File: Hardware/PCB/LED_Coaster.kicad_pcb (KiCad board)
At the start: 2 copper layers, 90 x 90 mm, 88 parts, among them J1 Li-po, J3 USB_C_Receptacle_USB2.0_16P, J4 UART, Q1 AO3401A, SW1 SW_SPDT, U1 ESP32-C3-WROOM-02-H4, U3 MCP73871-2CC, U4 TLV75533PDBVR

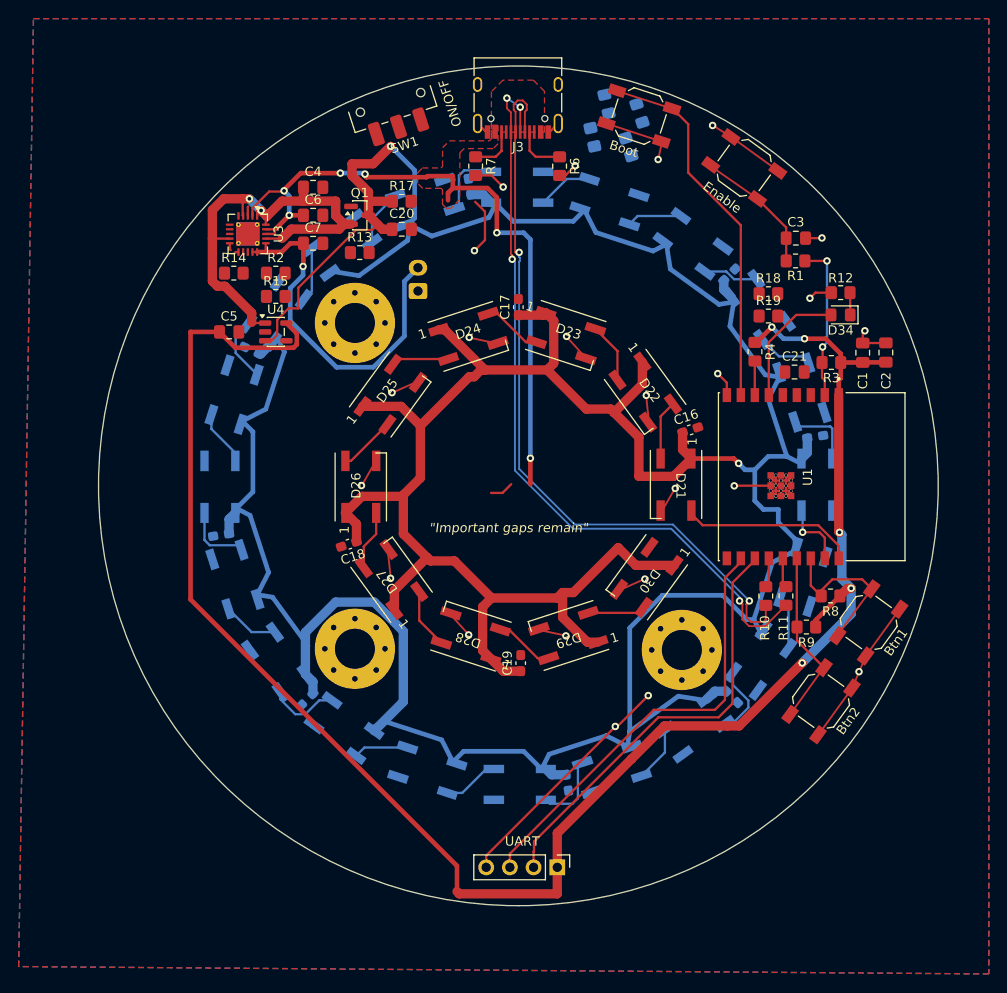
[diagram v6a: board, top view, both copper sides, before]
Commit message: Finish phase 5: route what was left and clean the board up
Every net with more than one pad is now one island, there are no
shorts, both LED chains are continuous, and the strays sweep is clean.

Routing:

- Action 8 in full - U3's three config resistors, the P-FET gate,
  R13 onto +SYS, both status LEDs across to R5/R16/D33/D35, and the
  battery-sense divider.
- A B.Cu link between J3's two VBUS pad pairs. They had only ever been
  joined by the priority-1 +5V zone, and when that zone shrank on a
  refill the status LEDs went with it - +5V split in two. The whole
  USB signal row sits between the pads and the F.Cu escapes below are
  taken by CC1, CC2 and the differential pairs, so the link runs
  underneath on B.Cu where there is nothing but the STAT2 run.
- U3 pad 3 down into U3's own exposed pad. Its old stub ran the other
  way and stopped 1.7 mm short of the pour, and the direct path to the
  pour crosses +SYS.

GND pad connection is now Solid, with thermal relief kept on J1, J3
and J4. Thermal relief was leaving eleven ground pads unconnected: the
pour was wrapped right around them at exactly thermal_gap, but the ring
traces block the spoke directions and KiCad places no spoke at all
rather than fewer than min_resolved_spokes. Reflow does not care about
solid pads; the three parts that get hand-soldered keep their relief.

min_copper_edge_clearance goes from 0.0 to 0.3 so the rule can actually
fail.

Also strips 14 items of junk copper: 12 zero-length segments and two
dangling stubs. All verified against connectivity before removal.

Co-Authored-By: Claude Opus 5 <noreply@anthropic.com>
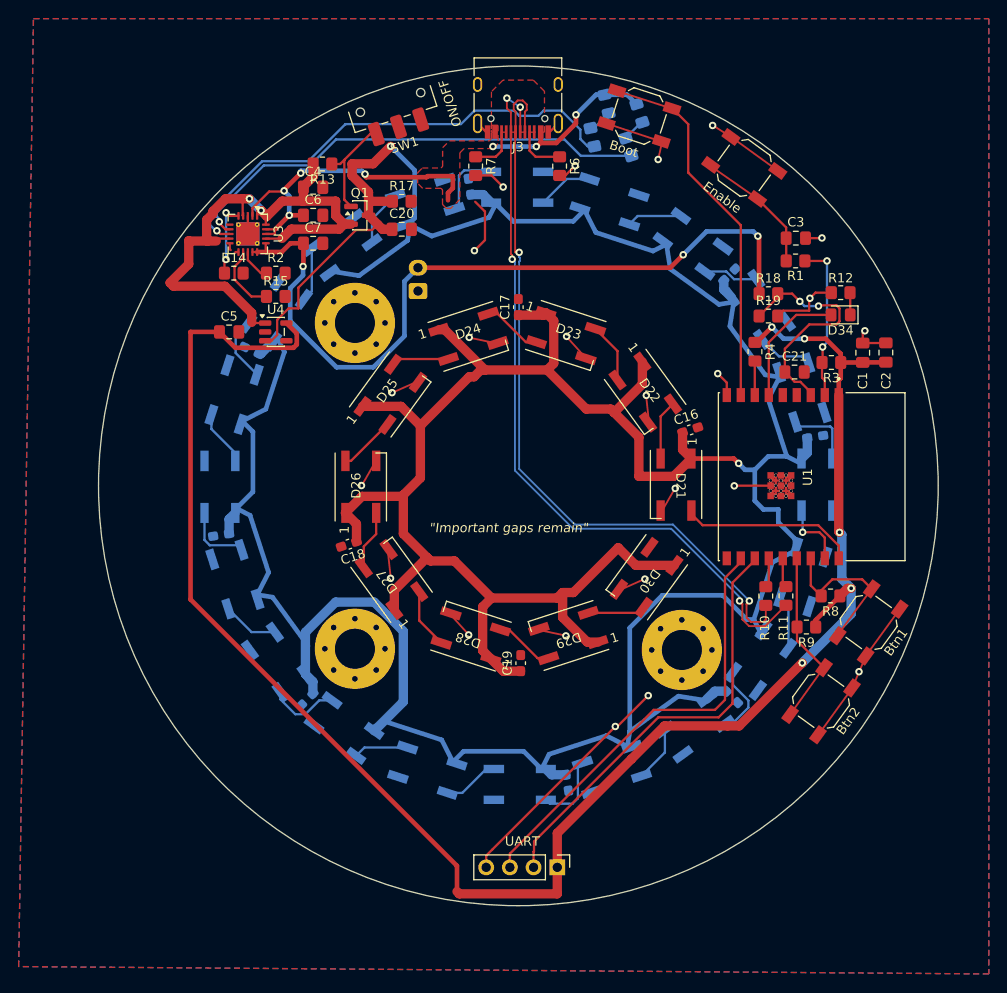
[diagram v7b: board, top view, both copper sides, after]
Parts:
- moved R13 10.3 mm to (129.0, 45.5), turned to 180 degrees
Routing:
- net Net-(U3-STAT1/~{LBO}): track 0.00 -> 52.3 mm, vias 0 -> 1
- net Net-(U3-STAT2): track 0.00 -> 51.1 mm, vias 0 -> 1
- net +BATT: track 39.4 -> 83.9 mm, vias 1 -> 3
- net /BAT_SENSE: track 0.00 -> 25.5 mm, vias 0 -> 2
- net +5V: track 75.2 -> 56.4 mm, vias 6 -> 7
- net Net-(Q1-G): track 0.00 -> 11.4 mm
- net +SYS: track 50.4 -> 61.7 mm
- net Net-(U3-THERM): track 0.00 -> 8.01 mm, vias 0 -> 2
- net Net-(U3-PROG3): track 0.00 -> 7.51 mm
- net GND: track 74.3 -> 80.2 mm
- net Net-(U3-PROG1): track 0.00 -> 3.44 mm
- net Net-(D35-K): track 0.00 -> 2.50 mm
